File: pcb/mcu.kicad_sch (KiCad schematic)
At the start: 15 parts, among them J3 Conn_02x03_Counter_Clockwise, J4 Conn_01x07, J5 Conn_01x07, SW6 SW_Push, U3 STM32F042K6Tx, U4 TLV70033_SOT23-5

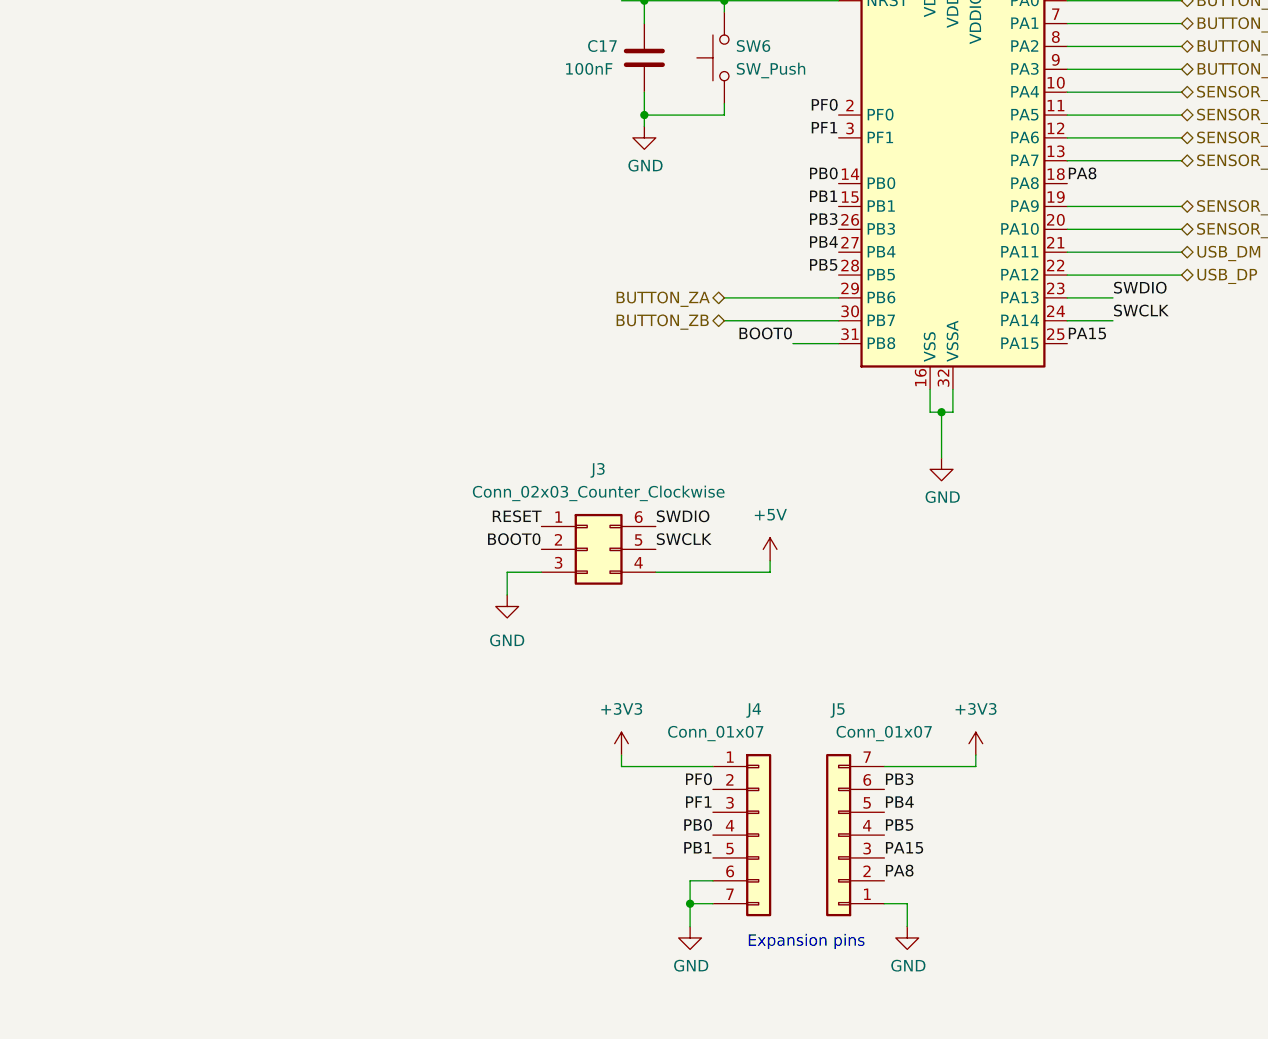
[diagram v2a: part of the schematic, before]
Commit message: added LCSC part numbers and assigned footprints
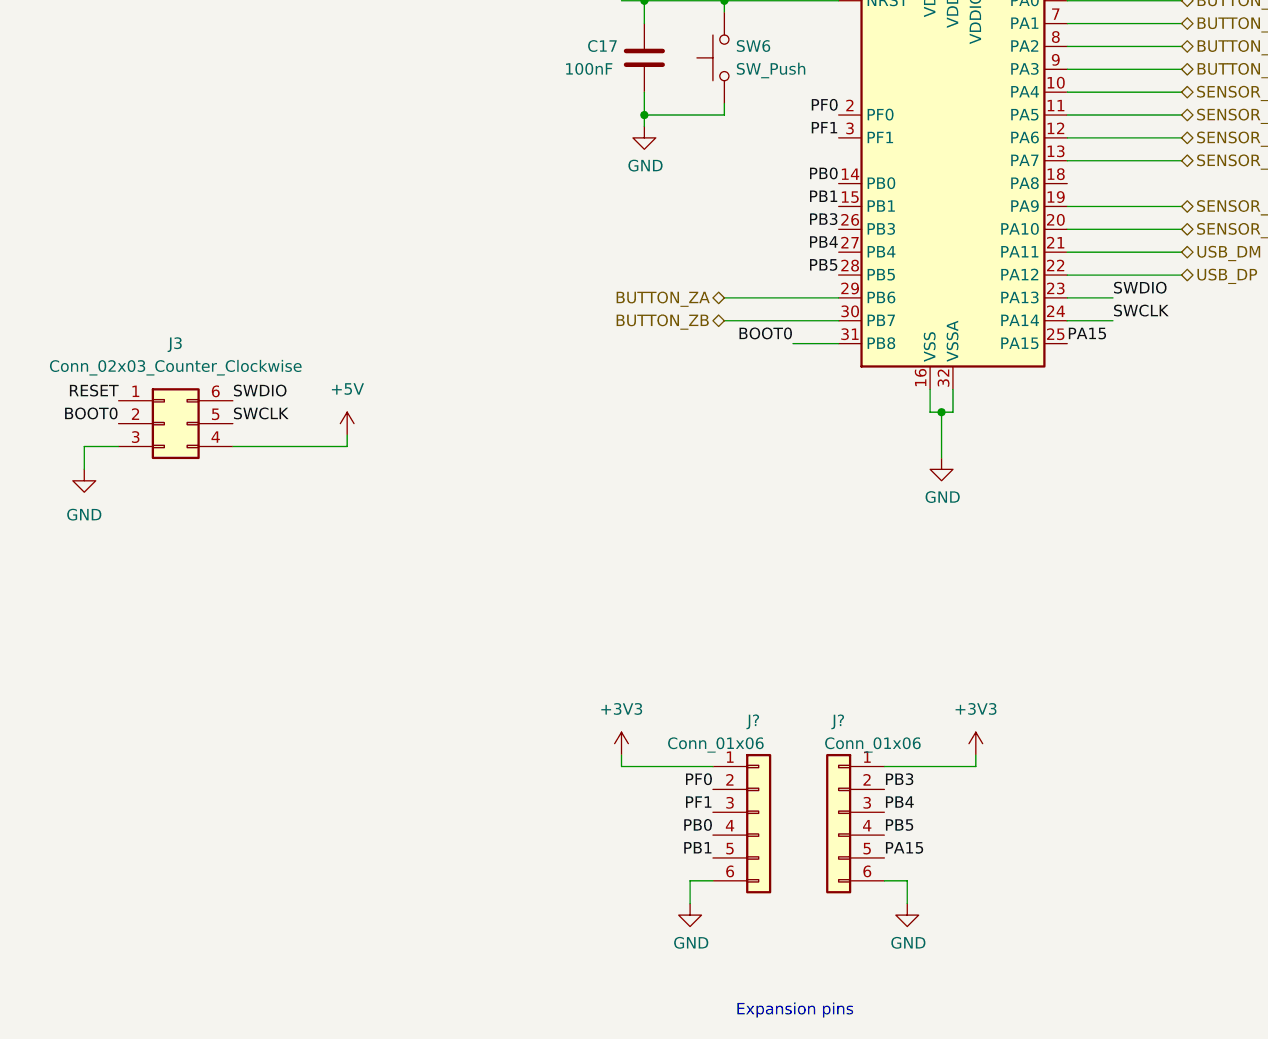
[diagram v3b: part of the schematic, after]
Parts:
- removed J4, J5: Conn_01x07, Connector_PinSocket_2.54mm:PinSocket_1x07_P2.54mm_Vertical, symbol Connector_Generic:Conn_01x07
- added J? (x2): Conn_01x06, symbol Connector_Generic:Conn_01x06
- C17, C20, C22: LCSC (none) -> C14663
- C18, C21: LCSC (none) -> C19666
- C19, C23, C24: LCSC (none) -> C15849
- C25: LCSC (none) -> C57112
- U3: LCSC (none) -> C69216
- U4: LCSC (none) -> C11337
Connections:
- net +3V3: now also J?.1 (Pin_1), J?.1 (Pin_1)
- net GND: now also J?.6 (Pin_6), J?.6 (Pin_6)
- net PA15: now also J?.5 (Pin_5)
- net PB0: now also J?.4 (Pin_4)
- net PB1: now also J?.5 (Pin_5)
- net PB3: now also J?.2 (Pin_2)
- net PB4: now also J?.3 (Pin_3)
- net PB5: now also J?.4 (Pin_4)
- net PF0: now also J?.2 (Pin_2)
- net PF1: now also J?.3 (Pin_3)
- net PA8: no longer names the net of U3.18 (PA8)
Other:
- moved on the sheet: J3

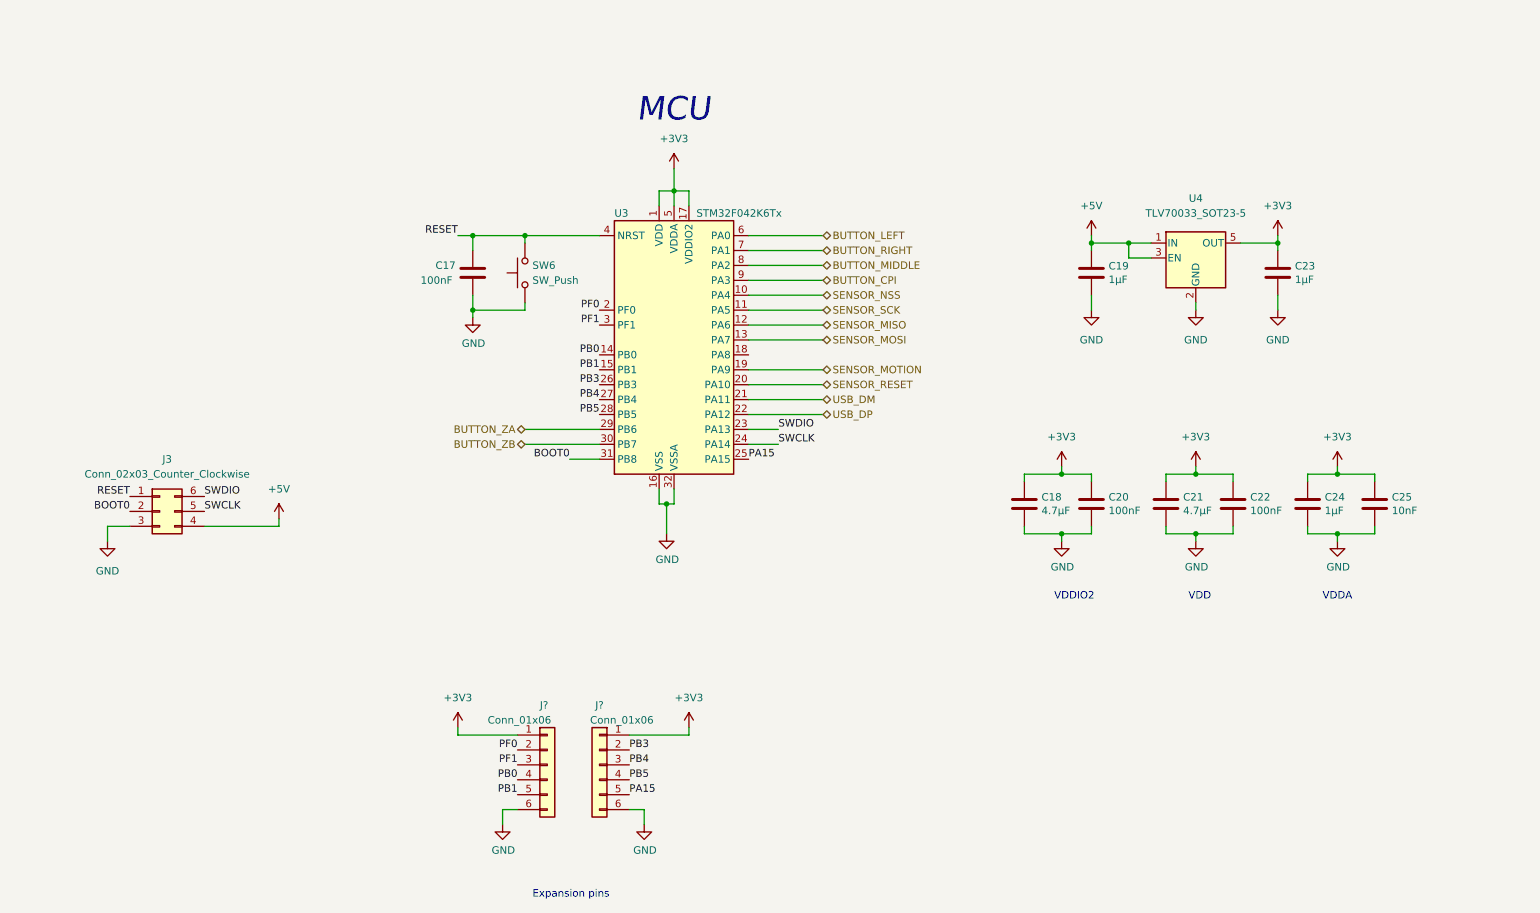
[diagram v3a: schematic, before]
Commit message: - added status leds - changed some lcsc components
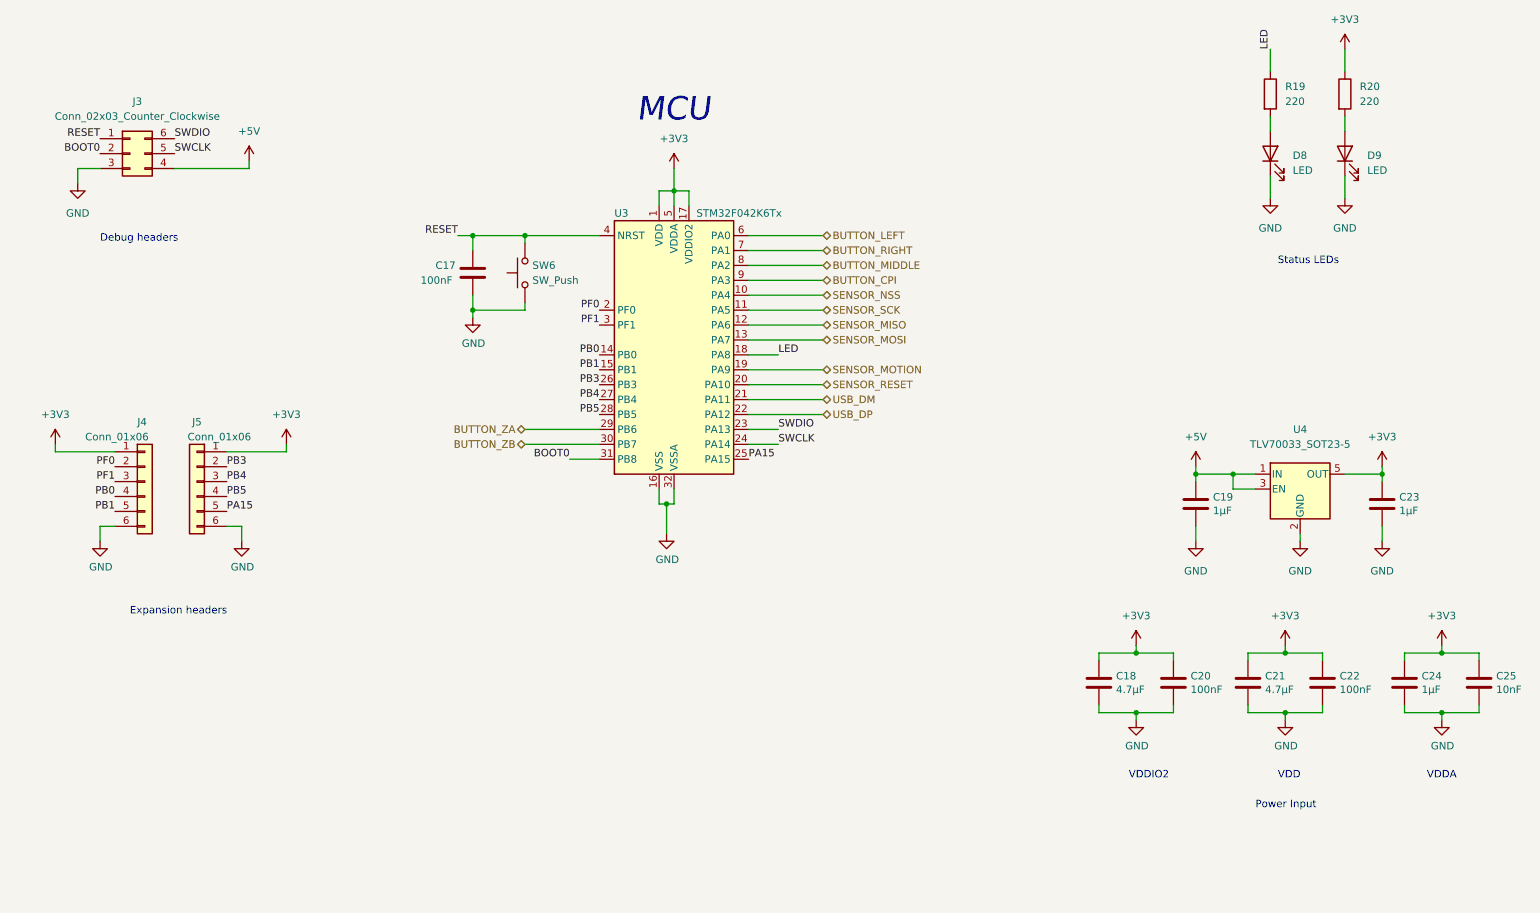
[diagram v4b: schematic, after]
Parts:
- added D8, D9: LED, LED_SMD:LED_0603_1608Metric, symbol Device:LED
- added R19, R20: 220, Resistor_SMD:R_0603_1608Metric, symbol Device:R
- J5: renamed from J?; footprint (none) -> Connector_PinSocket_2.54mm:PinSocket_1x06_P2.54mm_Vertical
- gave numbers to parts that had none: 1
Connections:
- net +3V3: now also R20.1
- net GND: now also D8.1 (K), D9.1 (K)
- net LED: now reaches U3.18 (PA8)
- net LED: now also R19.1
- new net: D8.2 (A), R19.2
- new net: D9.2 (A), R20.2
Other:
- note added: "Debug headers"
- note added: "Expansion headers"
- note added: "Power Input"
- note added: "Status LEDs"
- note removed: "Expansion pins"
- moved on the sheet: C18, C19, C20, C21, C22, C23, C24, C25, J3, J4, J5, U4

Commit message: - cleaned up schematics - roughly arranged components on pcb - added pcb outline
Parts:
- J4: footprint (none) -> Connector_PinSocket_2.54mm:PinSocket_1x06_P2.54mm_Vertical
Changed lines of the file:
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@@
       (effects (font (size 1.27 1.27)) (justify left))
     )
-    (property "Footprint" "" (id 2) (at 40.64 105.41 0)
+    (property "Footprint" "Connector_PinSocket_2.54mm:PinSocket_1x06_P2.54mm_Vertical" (id 2) (at 40.64 105.41 0)
       (effects (font (size 1.27 1.27)) hide)
     )
